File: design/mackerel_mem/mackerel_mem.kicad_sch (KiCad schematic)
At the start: 9 parts, among them U1 AS6C4008-55PCN, U2 AS6C4008-55PCN, U3 AS6C4008-55PCN, U4 AS6C4008-55PCN, U5 AS6C4008-55PCN, U6 AS6C4008-55PCN, U7 AS6C4008-55PCN, U8 AS6C4008-55PCN, U9 GAL16V8

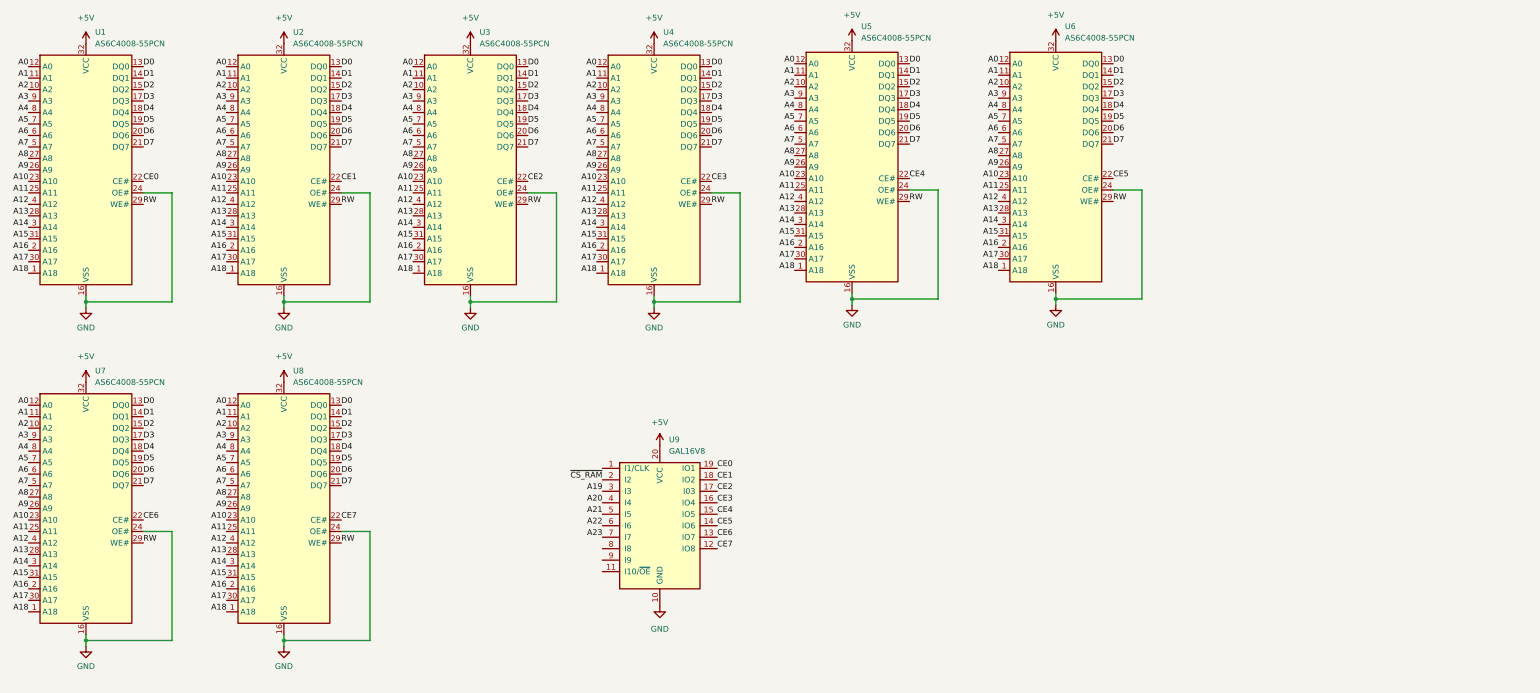
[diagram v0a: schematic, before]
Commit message: Defined system bus pinout and GAL decoding schematic
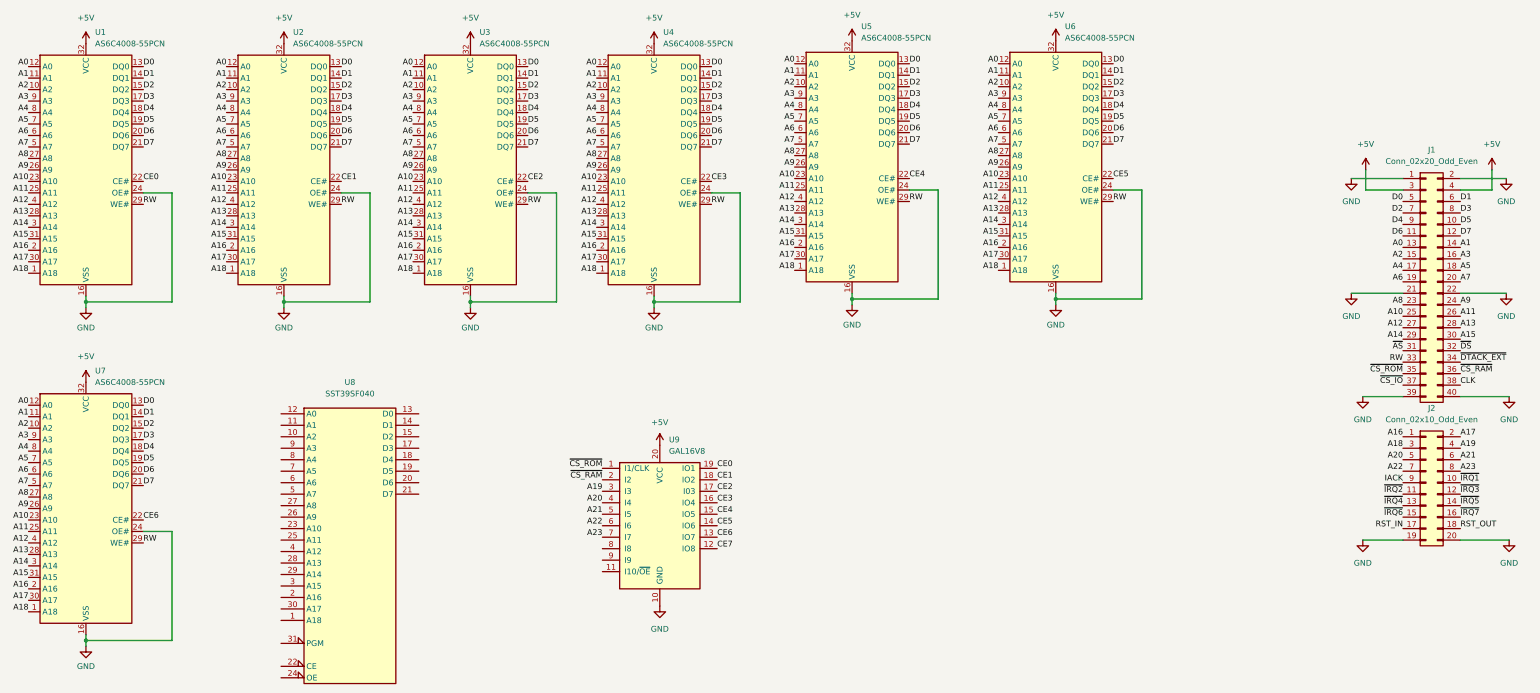
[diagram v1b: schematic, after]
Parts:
- removed U8: AS6C4008-55PCN, Package_DIP:DIP-32_W15.24mm, symbol Memory_RAM:AS6C4008-55PCN
- added J1: Conn_02x20_Odd_Even, Connector_PinSocket_2.54mm:PinSocket_2x20_P2.54mm_Horizontal, symbol Connector_Generic:Conn_02x20_Odd_Even
- added J2: Conn_02x10_Odd_Even, Connector_PinSocket_2.54mm:PinSocket_2x10_P2.54mm_Horizontal, symbol Connector_Generic:Conn_02x10_Odd_Even
- added U8: SST39SF040, Package_DIP:DIP-32_W15.24mm_Socket, symbol Memory_Flash:SST39SF040
- U1, U2, U3, U4, U5, U6, U7: footprint Package_DIP:DIP-32_W15.24mm -> Package_DIP:DIP-32_W15.24mm_Socket
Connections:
- net +5V: now also J1.3 (Pin_3), J1.4 (Pin_4)
- net A0: now also J1.13 (Pin_13)
- net A1: now also J1.14 (Pin_14)
- net A10: now also J1.25 (Pin_25)
- net A11: now also J1.26 (Pin_26)
- net A12: now also J1.27 (Pin_27)
- net A13: now also J1.28 (Pin_28)
- net A14: now also J1.29 (Pin_29)
- net A15: now also J1.30 (Pin_30)
- net A16: now also J2.1 (Pin_1)
- net A17: now also J2.2 (Pin_2)
- net A18: now also J2.3 (Pin_3)
- net A19: now also J2.4 (Pin_4)
- net A2: now also J1.15 (Pin_15)
- net A20: now also J2.5 (Pin_5)
- net A21: now also J2.6 (Pin_6)
- net A22: now also J2.7 (Pin_7)
- net A23: now also J2.8 (Pin_8)
- net A3: now also J1.16 (Pin_16)
- net A4: now also J1.17 (Pin_17)
- net A5: now also J1.18 (Pin_18)
- net A6: now also J1.19 (Pin_19)
- net A7: now also J1.20 (Pin_20)
- net A8: now also J1.23 (Pin_23)
- net A9: now also J1.24 (Pin_24)
- net D0: now also J1.5 (Pin_5)
- net D1: now also J1.6 (Pin_6)
- net D2: now also J1.7 (Pin_7)
- net D3: now also J1.8 (Pin_8)
- net D4: now also J1.9 (Pin_9)
- net D5: now also J1.10 (Pin_10)
- net D6: now also J1.11 (Pin_11)
- net D7: now also J1.12 (Pin_12)
- net GND: now also J1.1 (Pin_1), J1.2 (Pin_2), J1.21 (Pin_21), J1.22 (Pin_22), J1.39 (Pin_39), J1.40 (Pin_40), J2.19 (Pin_19), J2.20 (Pin_20), U8.16 (GND)
- net RW: now also J1.33 (Pin_33)
- net ~{CS_RAM}: now also J1.36 (Pin_36)
- net ~{CS_ROM}: now reaches U9.1 (I1/CLK)
- net ~{CS_ROM}: now also J1.35 (Pin_35)
- new net CLK: J1.38 (Pin_38)
- new net IACK: J2.9 (Pin_9)
- new net RST_IN: J2.17 (Pin_17)
- new net RST_OUT: J2.18 (Pin_18)
- new net VCC: U8.32 (VCC)
- new net ~{AS}: J1.31 (Pin_31)
- new net ~{CS_IO}: J1.37 (Pin_37)
- new net ~{DS}: J1.32 (Pin_32)
- new net ~{DTACK_EXT}: J1.34 (Pin_34)
- new net ~{IRQ1}: J2.10 (Pin_10)
- new net ~{IRQ2}: J2.11 (Pin_11)
- new net ~{IRQ3}: J2.12 (Pin_12)
- new net ~{IRQ4}: J2.13 (Pin_13)
- new net ~{IRQ5}: J2.14 (Pin_14)
- new net ~{IRQ6}: J2.15 (Pin_15)
- new net ~{IRQ7}: J2.16 (Pin_16)
